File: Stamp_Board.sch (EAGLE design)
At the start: 21 parts

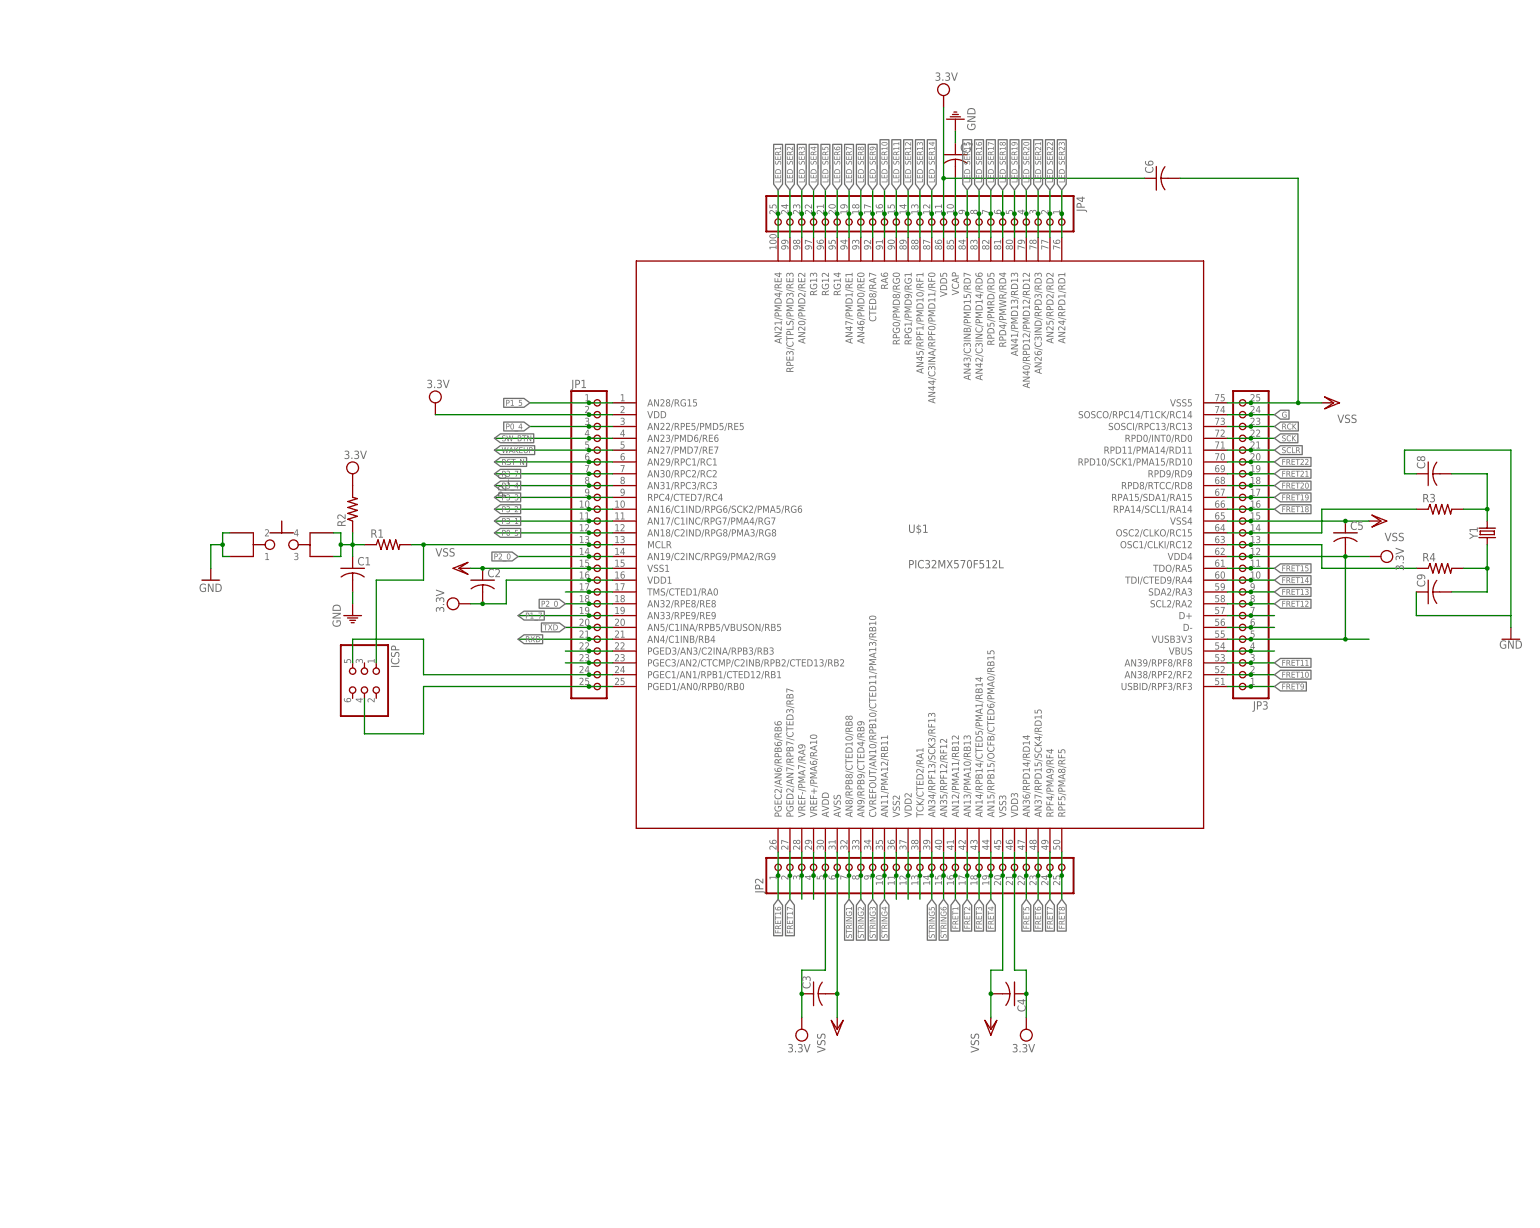
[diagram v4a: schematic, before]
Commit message: Added more caps because of PIC32 recommended connection. Updated and finished PCB layout. Added LDO to regulate input voltage.
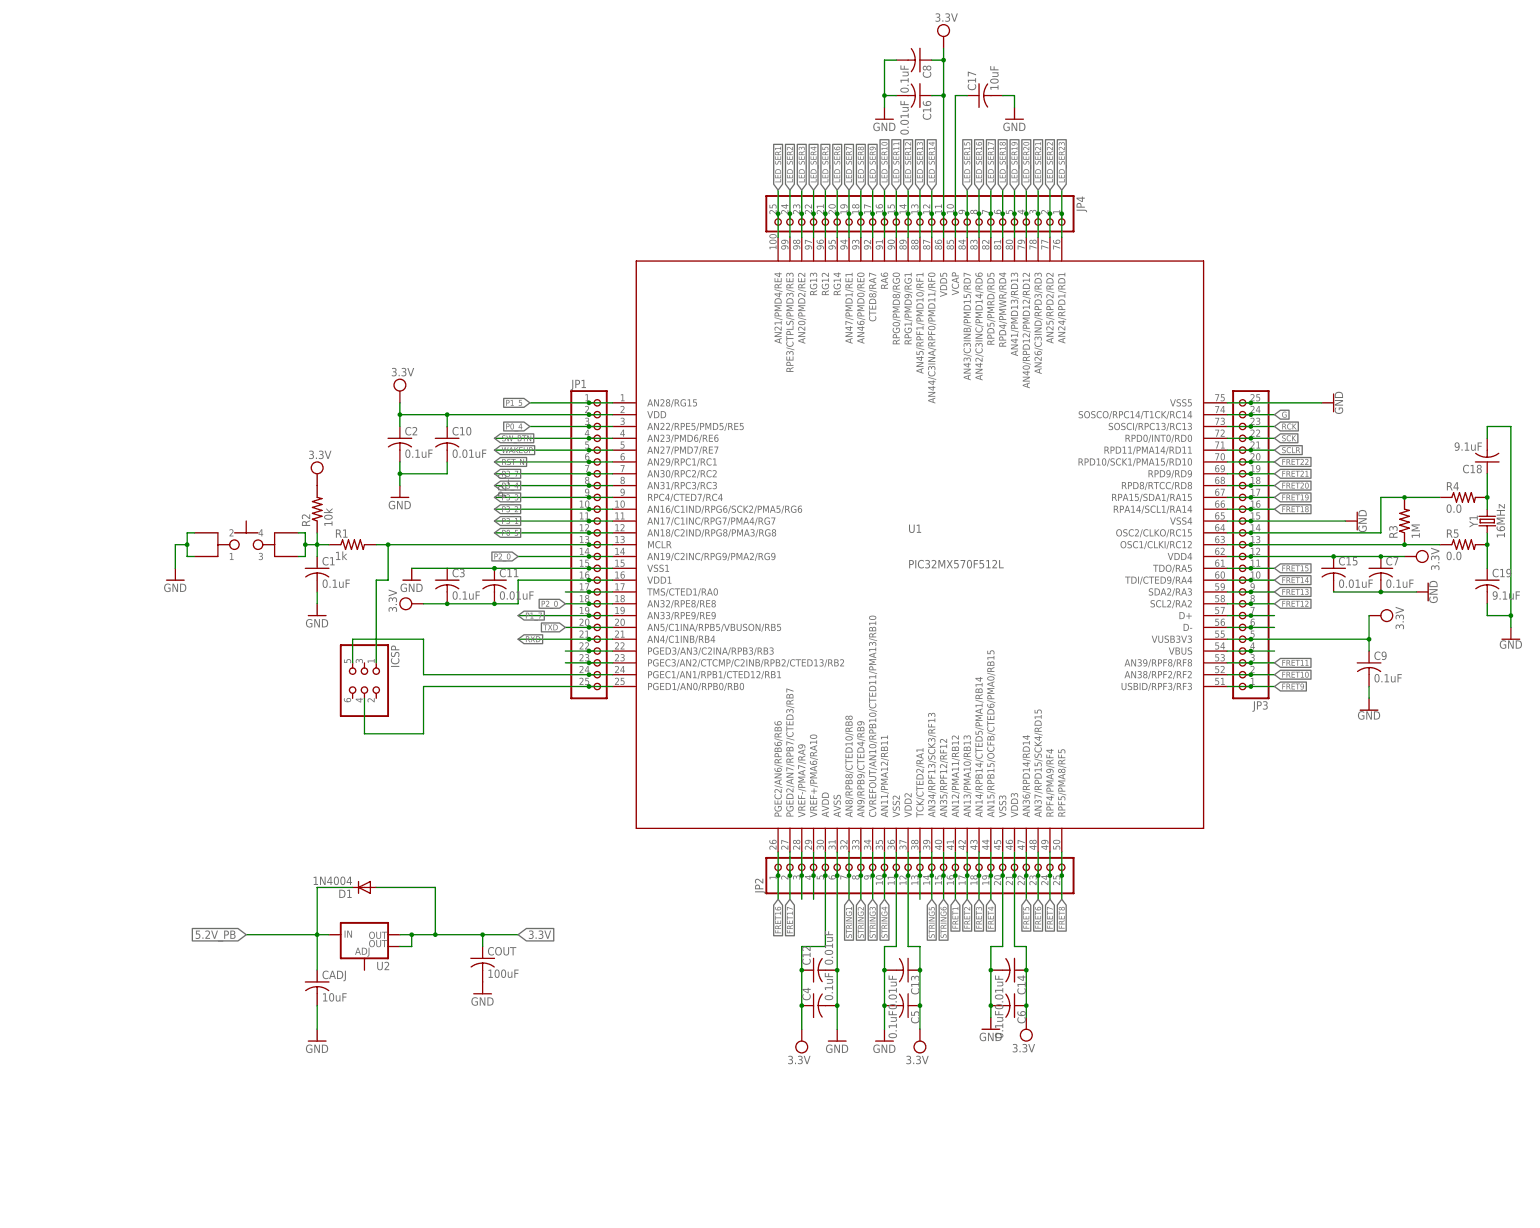
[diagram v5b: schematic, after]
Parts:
- removed U$2: LL3301NF065QG, ECE477_Guitutar:LL3301NF065QG
- added C10, C11, C12, C13, C14, C15, C16: 0.01uF, rcl:C-USC0805
- added C17, CADJ: 10uF, rcl:C-USC0805
- added C18, C19: 9.1uF, rcl:C-USC0805
- added COUT: 100uF, rcl:C-USC0805
- added D1: 1N4004, diode:1N4004
- added R5: 0.0, rcl:R-US_R0805
- added S1: LL3301NF065QG, ECE477_Guitutar:LL3301NF065QG
- added U2: (no value), SparkFun-IC-Power:V_REG_LM1117SOT223
- C1, C2, C3, C4, C5, C6, C7, C8, C9: value (none) -> 0.1uF
- R1: value (none) -> 1k
- R2: value (none) -> 10k
- R3: value (none) -> 1M
- R4: value (none) -> 0.0; device rcl:R-US_M0805 -> rcl:R-US_R0805
- Y1: value (none) -> 16MHz
- renumbered U$1 to U1
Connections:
- removed net N$11: JP3.14, R3.1, U1.OSC2/CLKO/RC15
- removed net N$50: JP2.11, U1.VSS2
- removed net N$51: JP2.12, U1.VDD2
- removed net VSS: C2.1, C3.2, C4.2, C5.1, C6.2, JP1.15, JP2.20, JP2.6, JP3.15, JP3.25, U1.AVSS, U1.VSS1, U1.VSS3, U1.VSS4, U1.VSS5
- new net 3.3V: COUT.1, D1.A, U2.OUT, U2.OUT@1
- new net 5.2V_PB: CADJ.1, D1.C, U2.IN
- new net N$1: JP3.14, R3.2, R4.1, U1.OSC2/CLKO/RC15
- net GND: now also C10.2, C11.1, C12.2, C13.2, C14.2, C15.2, C16.2, C17.2, C18.2, C19.2, C2.2, C3.1, C4.2, C5.2, C6.2, C7.2, C8.2, C9.2, CADJ.2, COUT.2, JP1.15, JP2.11, JP2.20, JP2.6, JP3.15, JP3.25, S1.1, S1.2, U1.AVSS, U1.VSS1, U1.VSS2, U1.VSS3, U1.VSS4, U1.VSS5; no longer C7.1, C8.1, C9.1, U$2.1, U$2.2
- net N$12: now also C17.1; no longer C7.2
- net N$15: now also R3.1, R5.1; no longer R4.1
- net N$16: now also S1.3, S1.4; no longer U$2.3, U$2.4
- net N$6: now also C18.1, R4.2; no longer C8.2, R3.2
- net N$8: now also C19.1, R5.2; no longer C9.2, R4.2
- net VDD: now also C10.1, C11.2, C12.1, C13.1, C14.1, C15.1, C16.1, C2.1, C3.2, C5.1, C7.1, C8.1, C9.1, JP2.12, U1.VDD2; no longer C2.2, C3.1, C5.2
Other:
- moved on the sheet: C1, C2, C3, C4, C5, C6, C7, C8, C9, R1, R2, R3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
